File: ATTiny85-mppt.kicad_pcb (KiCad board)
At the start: 2 copper layers, 97.6 x 90.8 mm, 50 parts, among them Q1 BUK9511-55A127, Q2 BUK9511-55A127, Q4 2N2222A, Q5 2N2907A, U1 LM7805_TO220, U2 LM358N, U3 ATtiny85-20PU

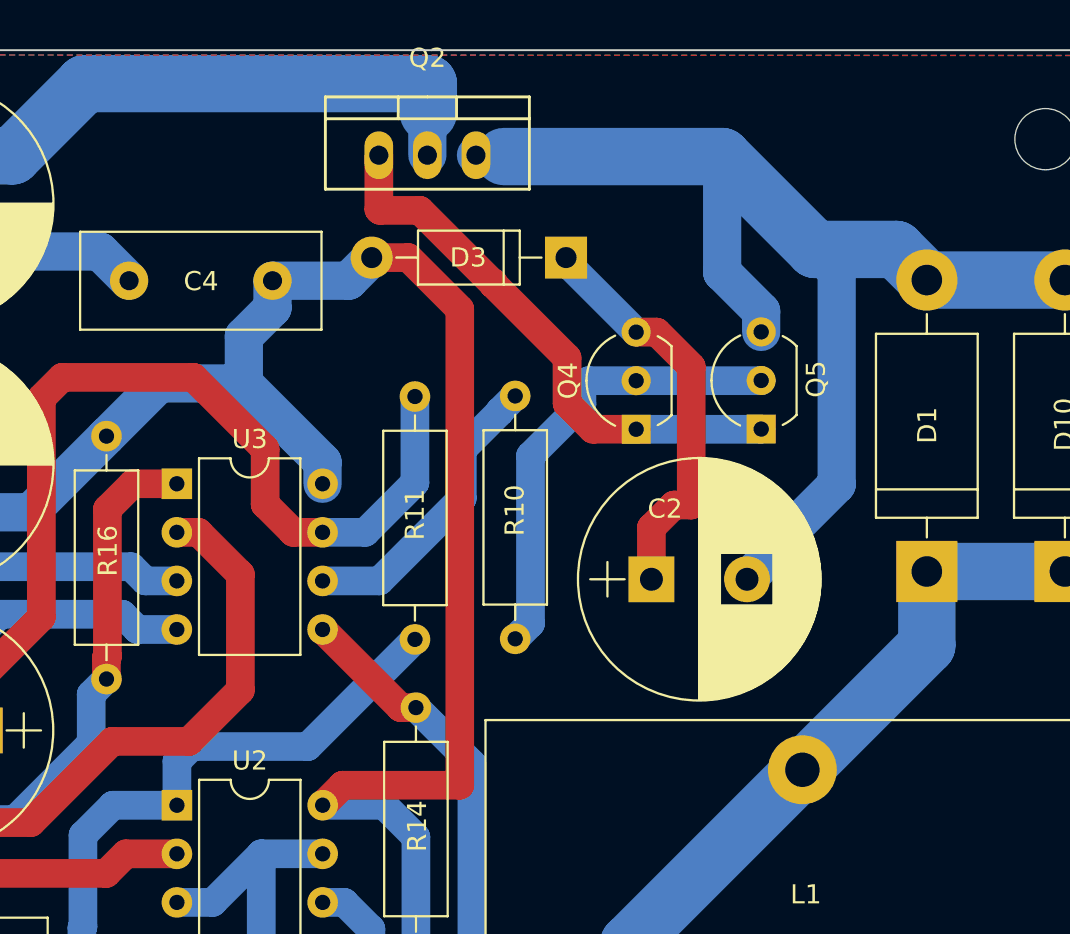
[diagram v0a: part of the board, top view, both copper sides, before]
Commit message: Fix circuit - FET Bootstrap don't work. Fix code - Inverting mode PWM.
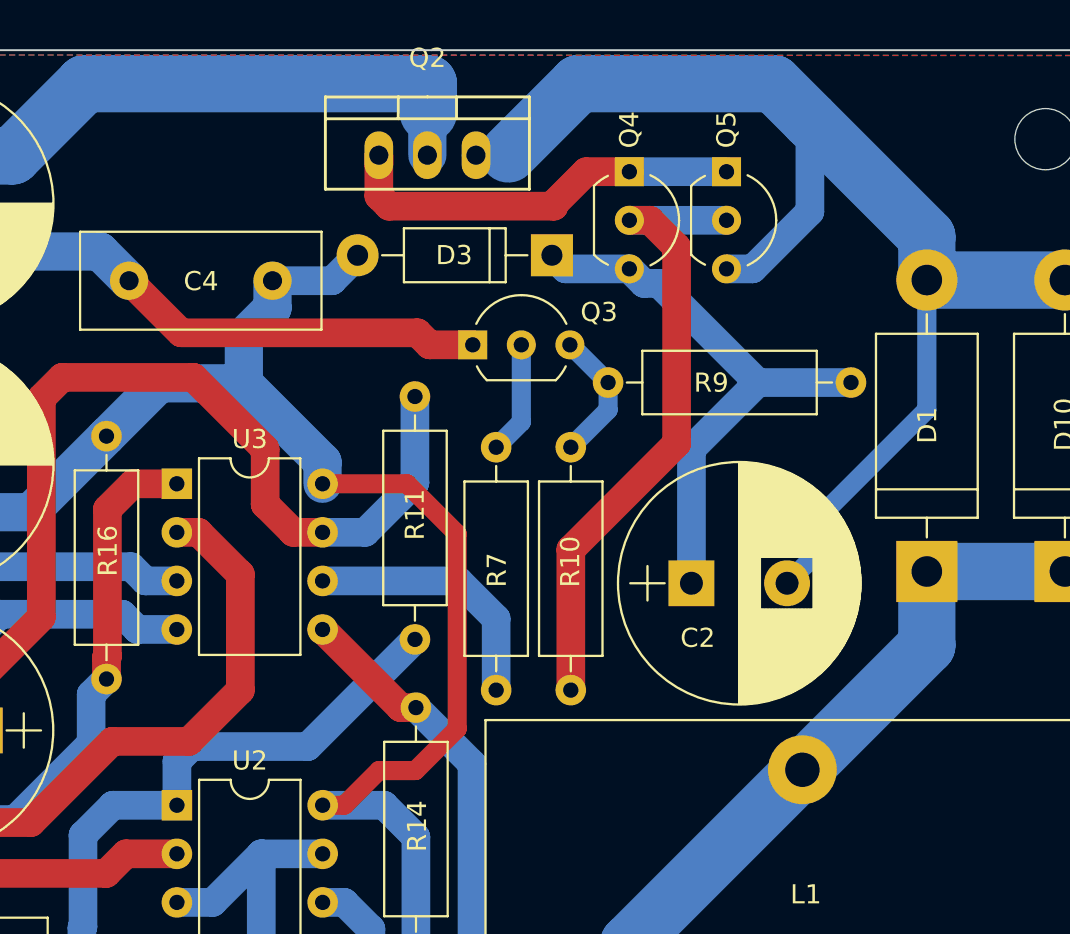
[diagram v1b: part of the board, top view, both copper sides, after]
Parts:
- added Q3: 2N2222A, TO_SOT_Packages_THT:TO-92_Inline_Wide, F.Cu at (107.9, 38.5)
- added R7: 1k, Resistors_THT:R_Axial_DIN0309_L9.0mm_D3.2mm_P12.70mm_Horizontal, F.Cu at (109.1, 56.5)
- added R9: 10k, Resistors_THT:R_Axial_DIN0309_L9.0mm_D3.2mm_P12.70mm_Horizontal, F.Cu at (114.9, 40.4)
- moved Q5 13.6 mm to (121.1, 29.4), turned to 270 degrees
- moved Q4 13.5 mm to (116.1, 29.4), turned to 270 degrees
- moved R10 3.95 mm to (113.0, 56.5)
- moved C2 2.10 mm to (119.3, 50.9)
- moved D3 0.75 mm to (112.0, 33.8)
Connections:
- R10 pad 2: /PWM -> Net-(Q3-Pad3)
- U3 pad 6: /PWM -> Net-(R7-Pad1)
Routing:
- net GND: track 251.7 -> 271.1 mm
- net /PWM: track 15.6 -> 0.00 mm
- net Net-(R7-Pad1): track 0.00 -> 13.6 mm
- net /BootStrap: track 98.3 -> 86.4 mm
- net Net-(Q4-Pad2): track 24.1 -> 33.6 mm
- net Net-(C2-Pad1): track 21.6 -> 30.3 mm
- net Net-(Q2-Pad1): track 29.1 -> 21.8 mm
- net Net-(Q3-Pad3): track 0.00 -> 7.00 mm
- net /~PWM: track 0.00 -> 5.90 mm
- net Net-(C2-Pad2): track 63.2 -> 67.2 mm

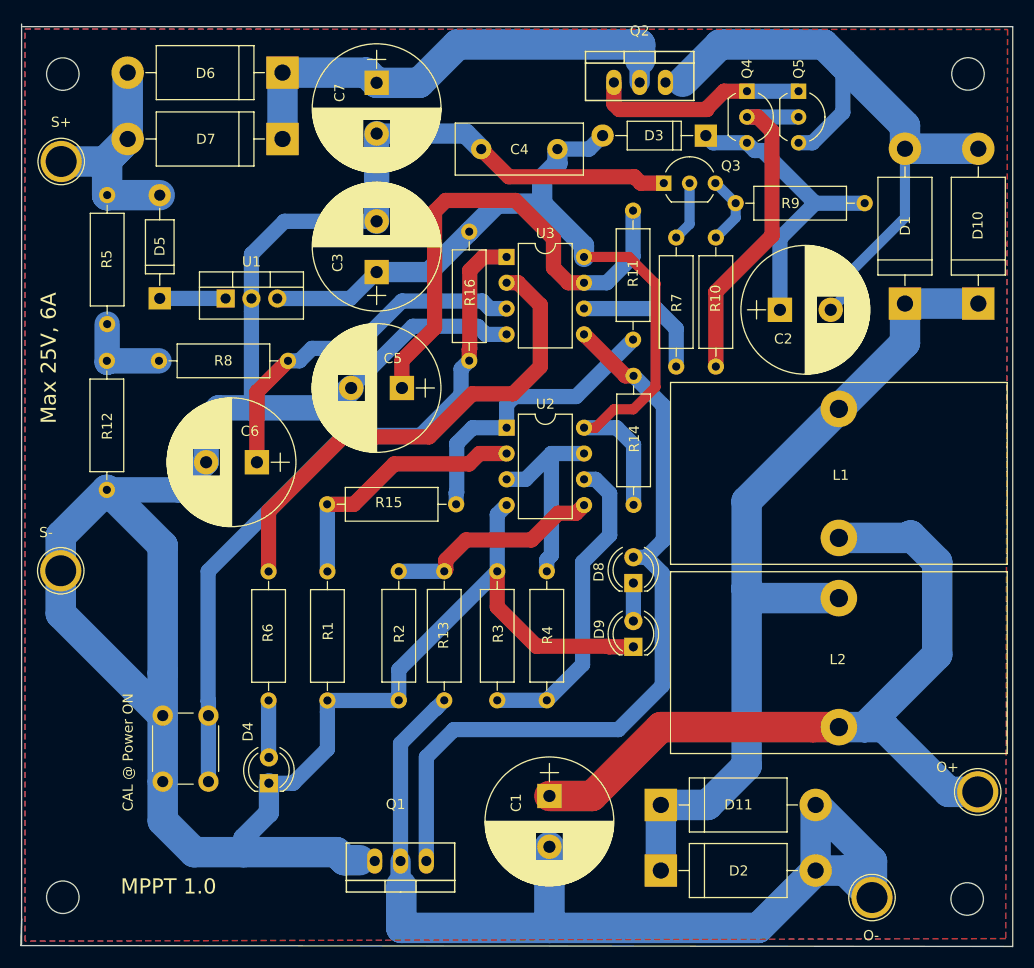
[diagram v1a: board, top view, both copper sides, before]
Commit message: Back to non-inverting. Fix FET Bootstrap.
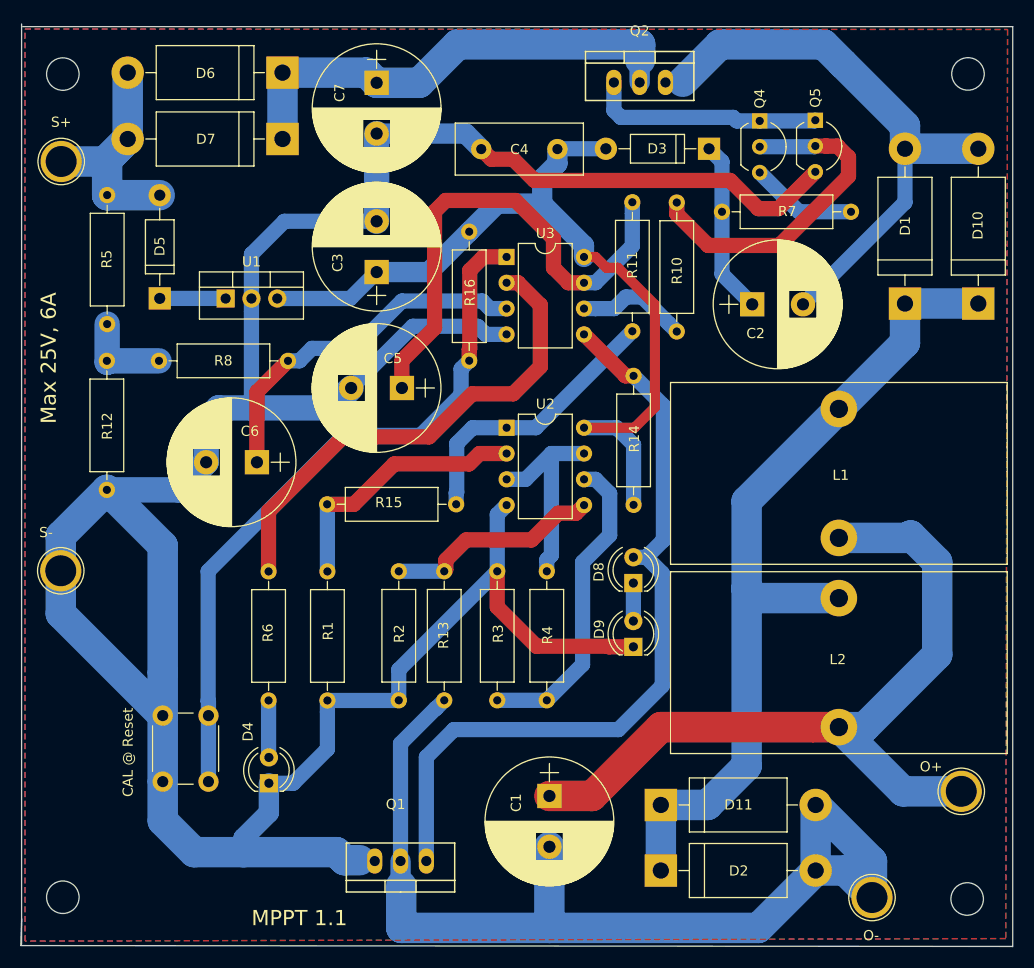
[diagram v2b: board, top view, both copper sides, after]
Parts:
- removed Q3: 2N2222A, TO_SOT_Packages_THT:TO-92_Inline_Wide
- removed R9: 10k, Resistors_THT:R_Axial_DIN0309_L9.0mm_D3.2mm_P12.70mm_Horizontal
- CAL @ Reset: renamed from CAL @ Power ON
- moved R7 23.0 mm to (126.3, 41.3), turned to 180 degrees
- moved R10 16.6 mm to (109.1, 40.4), turned to 270 degrees
- moved Q5 3.30 mm to (122.8, 32.3)
- moved Q4 3.18 mm to (117.3, 32.3)
- moved C2 2.78 mm to (116.6, 50.4)
- moved O+ 1.62 mm to (137.2, 98.3)
- moved D3 1.33 mm to (112.3, 35.1)
- moved R11 0.83 mm to (104.8, 53.0)
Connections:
- Q4 pad 3: Net-(C2-Pad1) -> Net-(Q4-Pad3)
- Q5 pad 3: Net-(C2-Pad2) -> GND
- R10 pad 2: Net-(Q3-Pad3) -> /PWM
- R7 pad 1: Net-(R7-Pad1) -> Net-(Q4-Pad3)
- R7 pad 2: /~PWM -> Net-(C2-Pad1)
- U3 pad 6: Net-(R7-Pad1) -> /PWM
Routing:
- net GND: track 271.1 -> 288.5 mm
- net Net-(R7-Pad1): track 13.6 -> 0.00 mm
- net Net-(C2-Pad1): track 30.3 -> 17.1 mm
- net /PWM: track 0.00 -> 11.0 mm
- net Net-(Q4-Pad3): track 0.00 -> 10.6 mm
- net Net-(C2-Pad2): track 67.2 -> 57.4 mm
- net Net-(Q3-Pad3): track 7.00 -> 0.00 mm
- net /~PWM: track 5.90 -> 0.00 mm
- net Net-(Q2-Pad1): track 21.8 -> 23.5 mm
- net /PV-Current: track 28.9 -> 27.9 mm
- net PRI_HI: track 77.7 -> 78.6 mm
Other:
- board text added: "MPPT 1.1"
- board text removed: "MPPT 1.0"

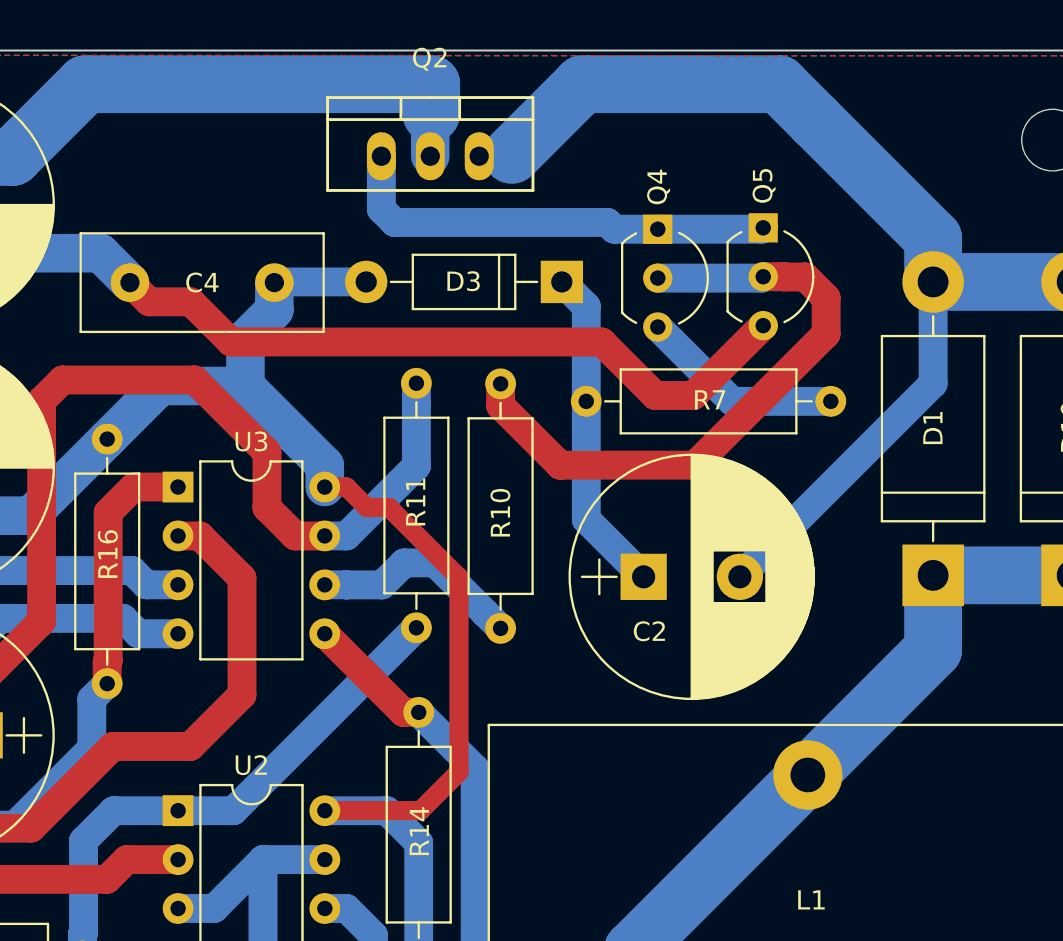
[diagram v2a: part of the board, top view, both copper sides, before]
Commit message: Fix by Invert Mode, 8Khz PWM. FET Bootstrap don't work with Higher frequency.
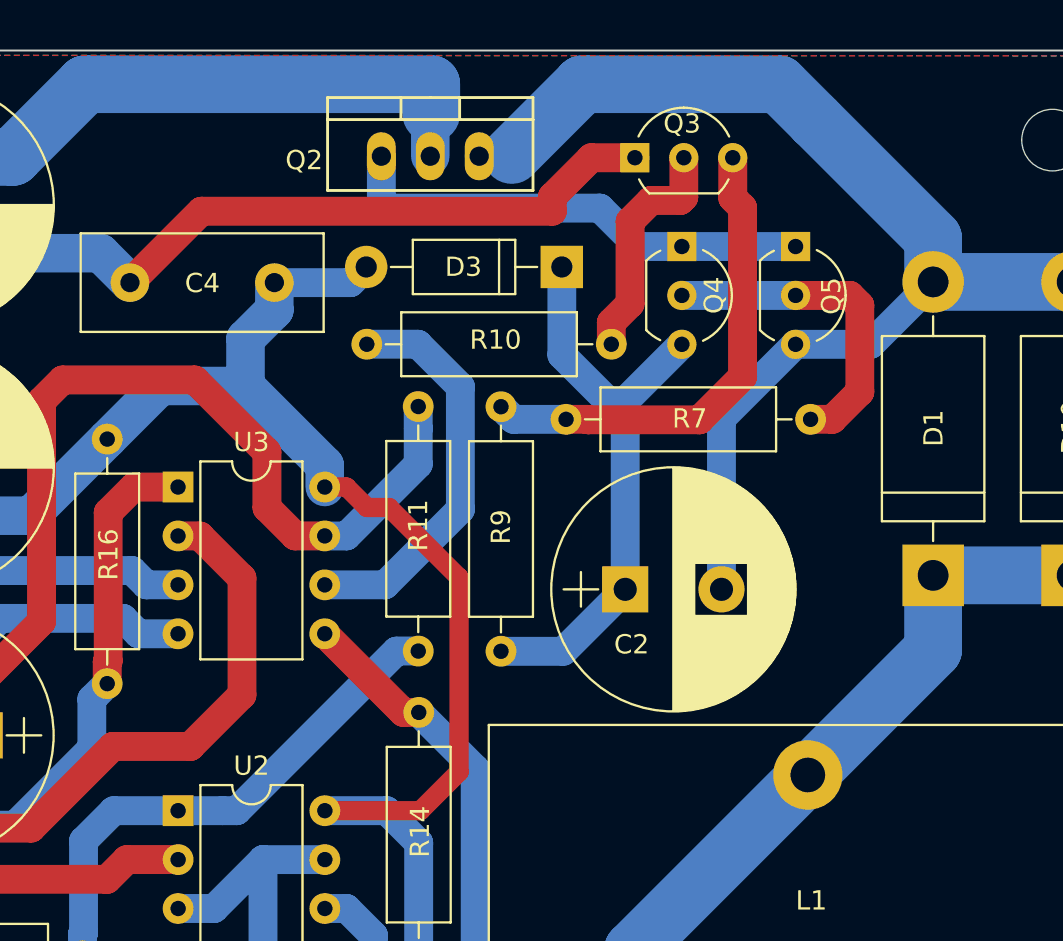
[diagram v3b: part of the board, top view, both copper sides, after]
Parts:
- added Q3: 2N2222A, TO_SOT_Packages_THT:TO-92_Inline_Wide, F.Cu at (116.1, 28.6)
- added R9: 10k, Resistors_THT:R_Axial_DIN0309_L9.0mm_D3.2mm_P12.70mm_Horizontal, F.Cu at (109.2, 41.6)
- Q5: value 2N2907A -> 2N2903A
- moved R10 7.25 mm to (102.2, 38.3), turned to 0 degrees
- moved Q5 1.94 mm to (124.5, 33.2)
- moved Q4 1.54 mm to (118.6, 33.2)
- moved R7 1.41 mm to (125.2, 42.2)
- moved R11 1.21 mm to (104.9, 54.2)
- moved C2 1.16 mm to (115.6, 51.0)
- moved D3 0.78 mm to (112.3, 34.3)
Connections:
- Q4 pad 3: Net-(Q4-Pad3) -> Net-(C2-Pad1)
- Q5 pad 3: GND -> Net-(C2-Pad2)
- R10 pad 1: Net-(Q4-Pad2) -> Net-(R10-Pad1)
- R10 pad 2: /PWM -> Net-(Q3-Pad2)
- R7 pad 1: Net-(Q4-Pad3) -> Net-(Q4-Pad2)
- R7 pad 2: Net-(C2-Pad1) -> Net-(Q3-Pad3)
- U3 pad 6: /PWM -> Net-(R10-Pad1)
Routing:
- net Net-(Q3-Pad3): track 0.00 -> 25.3 mm
- net Net-(R10-Pad1): track 0.00 -> 20.8 mm
- net Net-(Q4-Pad2): track 33.2 -> 17.1 mm
- net Net-(C2-Pad1): track 17.1 -> 30.6 mm
- net Net-(Q3-Pad2): track 0.00 -> 12.1 mm
- net /PWM: track 11.0 -> 0.00 mm
- net Net-(Q4-Pad3): track 10.6 -> 0.00 mm
- net GND: track 288.5 -> 281.1 mm
- net Net-(C2-Pad2): track 57.4 -> 60.7 mm
- net Net-(Q2-Pad1): track 23.5 -> 25.3 mm
- net Net-(C5-Pad1): track 49.5 -> 48.3 mm

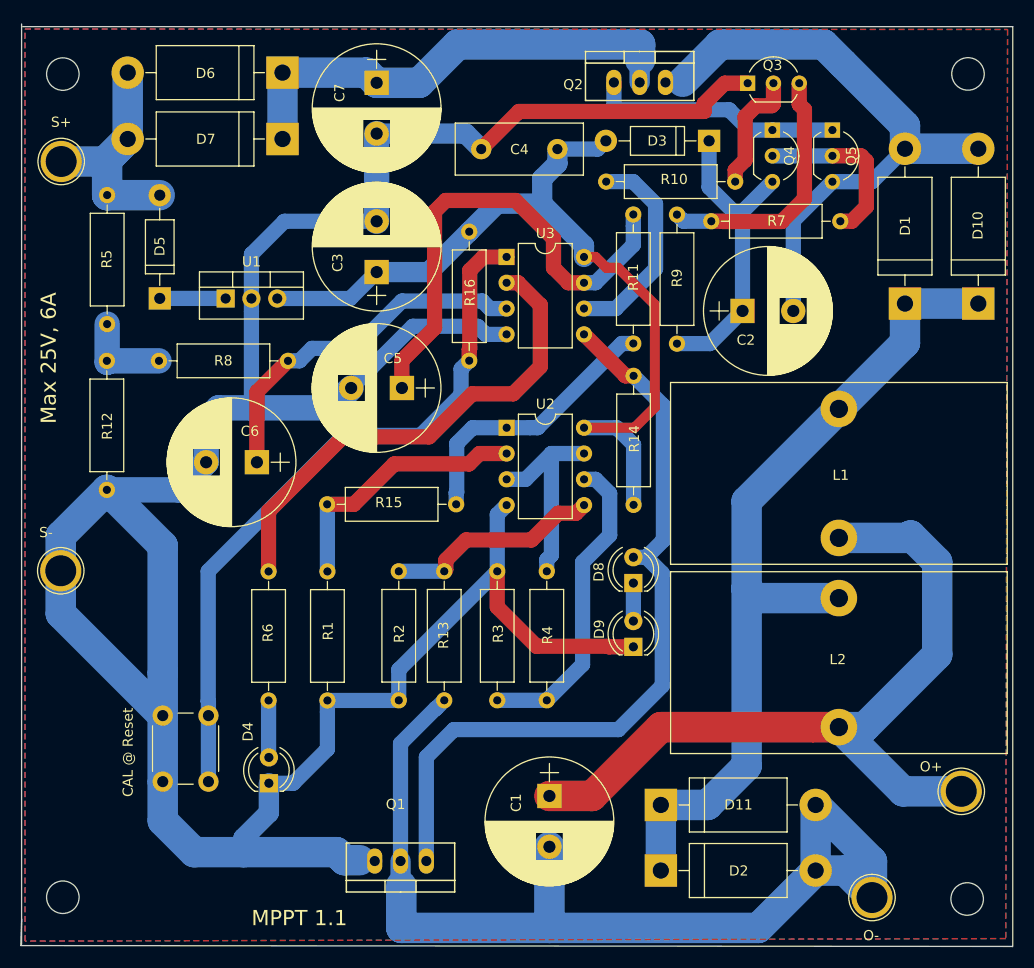
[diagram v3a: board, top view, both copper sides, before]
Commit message: Add another P FET for switching.
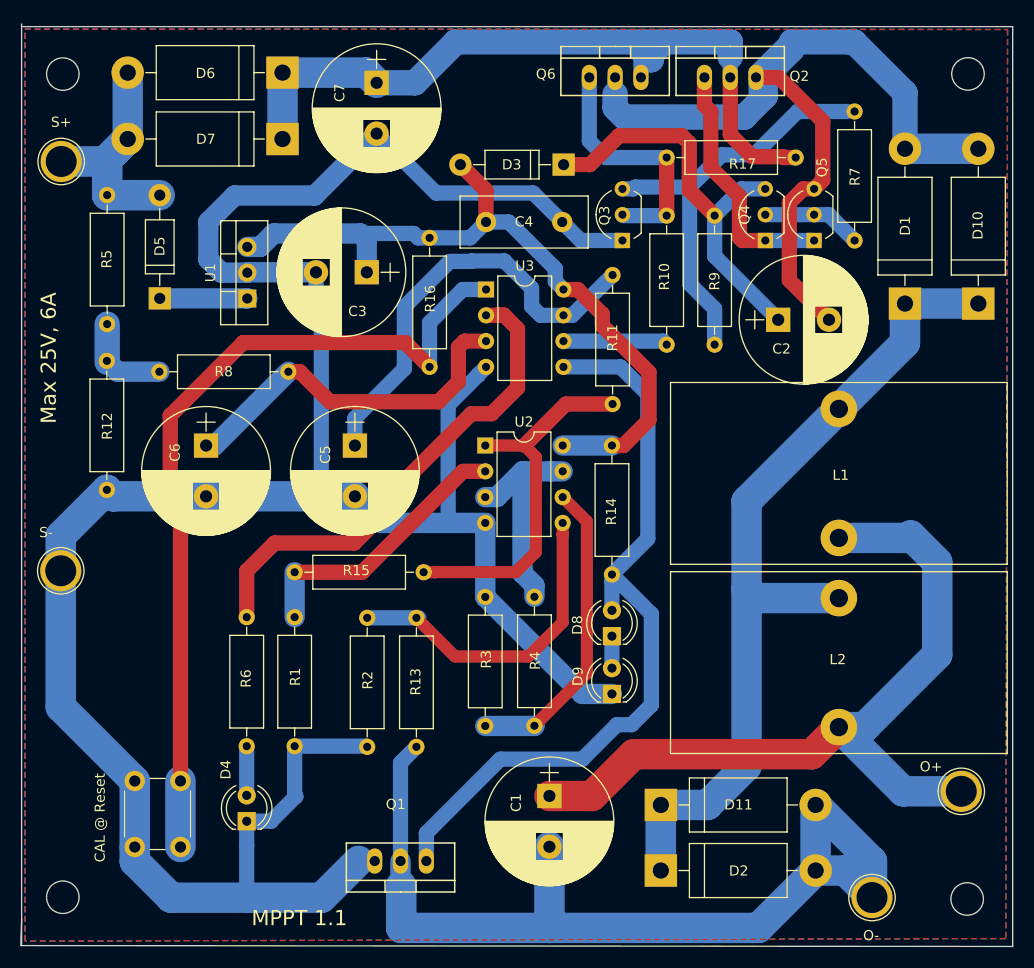
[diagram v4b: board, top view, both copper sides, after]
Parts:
- added Q6: BUK9508-55A, TO_SOT_Packages_THT-2:TO-220_Neutral123_Vertical, F.Cu at (103.1, 28.1)
- added R17: 1M, Resistors_THT:R_Axial_DIN0309_L9.0mm_D3.2mm_P12.70mm_Horizontal, F.Cu at (108.2, 35.9)
- C2: value 1u -> >10uF
- Q5: value 2N2903A -> 2N2904A
- moved Q3 19.8 mm to (103.8, 44.1), turned to 90 degrees
- moved R10 17.1 mm to (108.2, 54.4), turned to 90 degrees
- moved D3 14.5 mm to (98.0, 36.6)
- moved R9 13.3 mm to (112.9, 54.4), turned to 90 degrees
- moved Q5 11.0 mm to (122.7, 44.1), turned to 90 degrees
- moved Q4 10.9 mm to (117.9, 44.1), turned to 90 degrees
- moved C4 10.0 mm to (90.4, 42.3), turned to 0 degrees
- moved Q2 8.93 mm to (114.4, 28.1)
- moved R15 7.41 mm to (71.5, 76.8)
- moved C5 7.31 mm to (77.5, 64.3), turned to 270 degrees
- moved CAL @ Reset 7.00 mm to (55.8, 103.8)
- moved R11 6.30 mm to (102.8, 60.2)
- moved R14 6.22 mm to (102.8, 64.3), turned to 270 degrees
- moved D8 5.64 mm to (102.8, 83.1)
- moved R1 5.54 mm to (71.5, 93.9)
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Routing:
- net Net-(C7-Pad1): track 47.5 -> 103.5 mm
- net Net-(C2-Pad2): track 60.7 -> 93.2 mm
- net GND: track 281.1 -> 259.0 mm
- net Net-(Q3-Pad3): track 25.3 -> 41.8 mm
- net Net-(R16-Pad1): track 69.6 -> 83.7 mm
- net /BootStrap: track 86.3 -> 73.5 mm
- net Net-(Q3-Pad2): track 12.1 -> 24.7 mm
- net Net-(R13-Pad2): track 21.5 -> 32.2 mm
- net Net-(R10-Pad1): track 20.8 -> 10.3 mm
- net Net-(C2-Pad1): track 30.6 -> 40.9 mm
- net /PV-Current: track 27.5 -> 37.0 mm
- net Net-(Q4-Pad2): track 17.1 -> 9.85 mm
- net PRI_LO: track 99.9 -> 94.1 mm
- net Net-(C5-Pad1): track 48.3 -> 42.9 mm
- net Net-(D5-Pad1): track 6.49 -> 8.62 mm
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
